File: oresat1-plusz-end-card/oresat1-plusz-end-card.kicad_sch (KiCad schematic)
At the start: 35 parts, among them J1 J-SAMTEC-TFM-120-01-L-D-RA, J2 M55-7101242R, J3 M55-7101242R, J4 M55-7101242R, J5 M55-7101242R, J6 U.FL-R-SMT-1

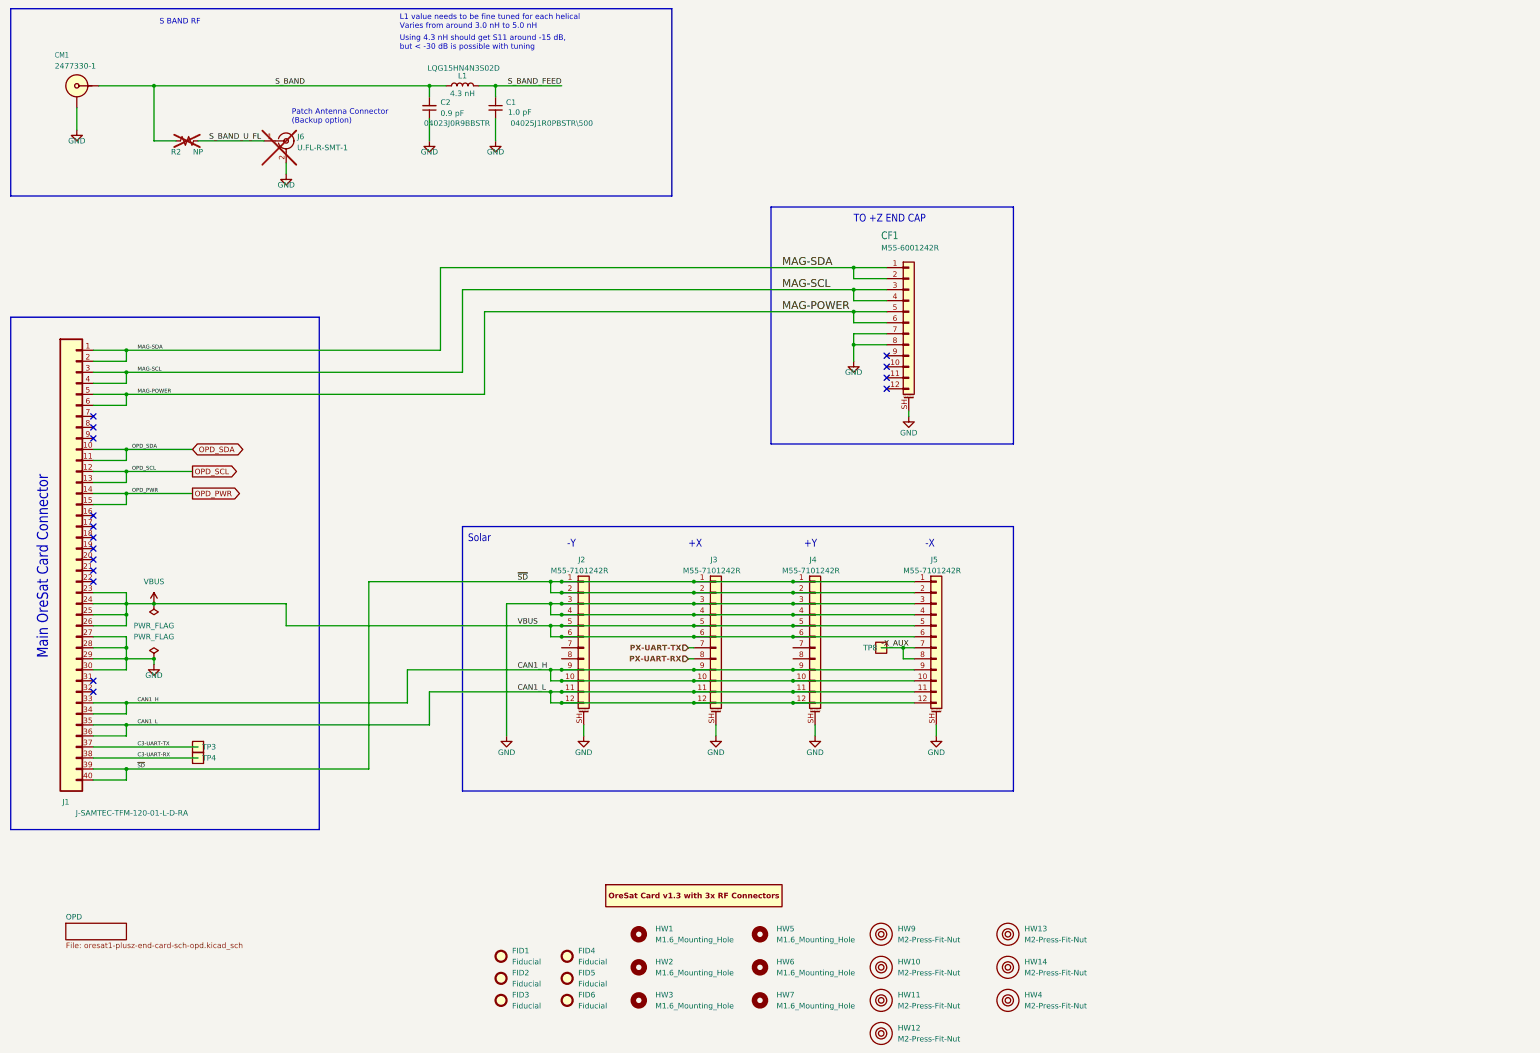
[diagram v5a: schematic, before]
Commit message: Fixed schematic label issues and routed solar uarts
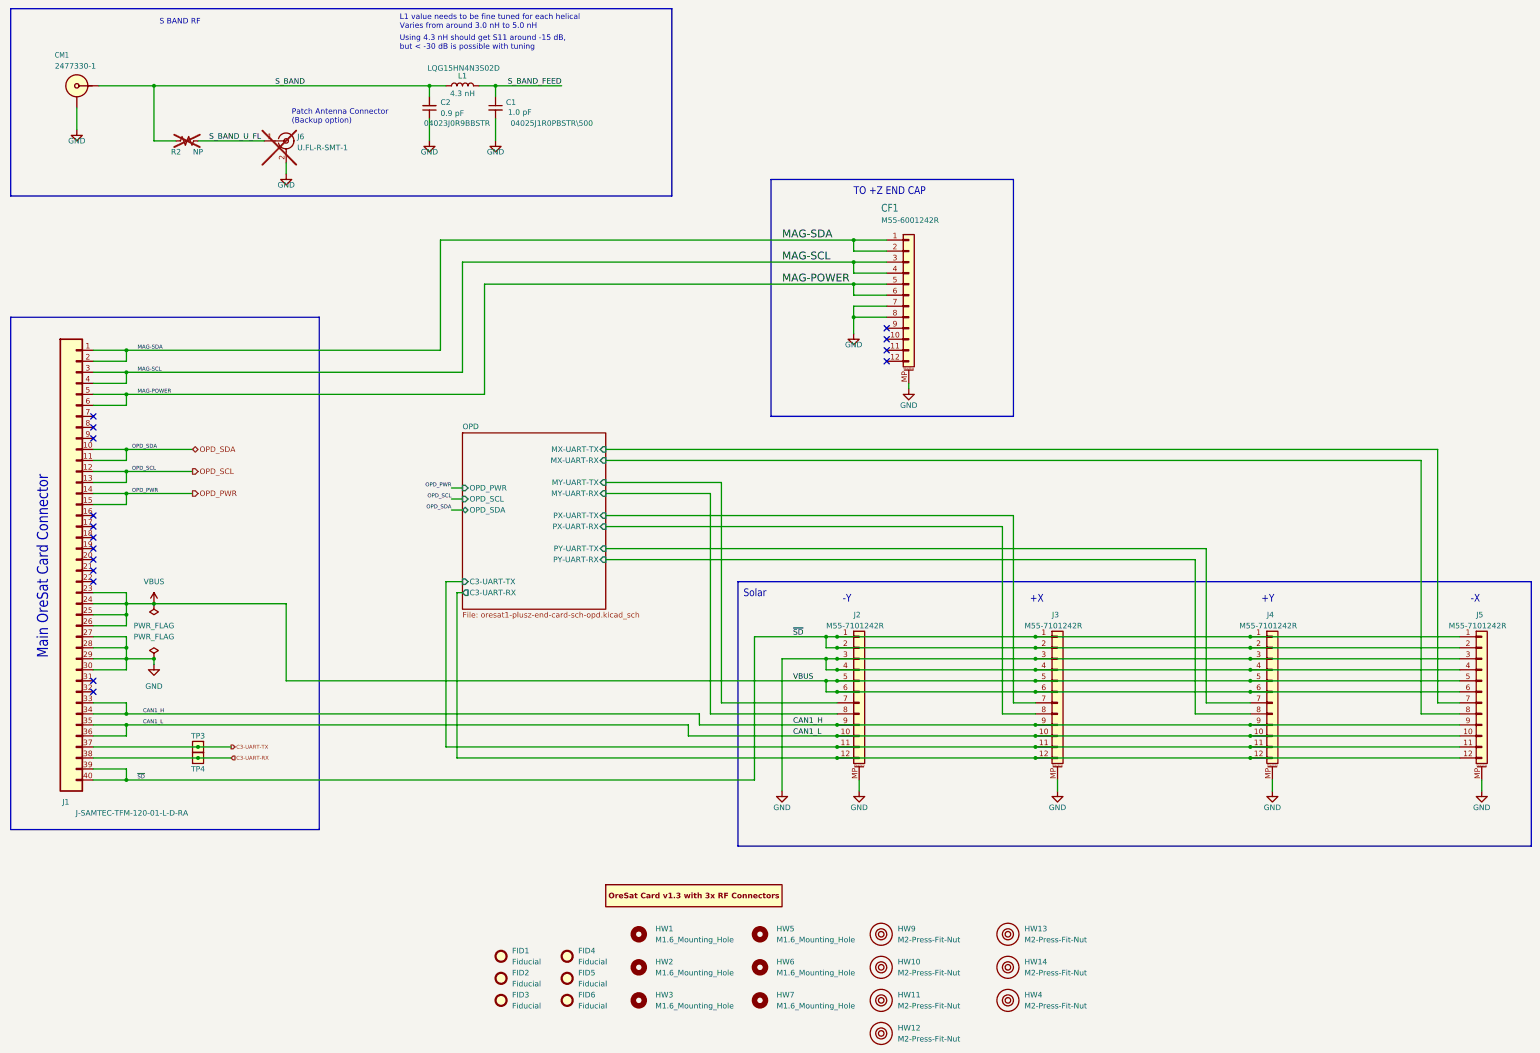
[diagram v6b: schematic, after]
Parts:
- removed TP8: TestPoint-MinTH, oresat-misc:TestPoint-0.75mm-th, symbol oresat-misc:Test-Point-0.75mm-th
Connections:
- net CAN1_H: no longer J2.10 (Pin_10), J3.10 (Pin_10), J4.10 (Pin_10), J5.10 (Pin_10)
- net CAN1_L: now also J2.10 (Pin_10), J3.10 (Pin_10), J4.10 (Pin_10), J5.10 (Pin_10); no longer J2.11 (Pin_11), J2.12 (Pin_12), J3.11 (Pin_11), J3.12 (Pin_12), J4.11 (Pin_11), J4.12 (Pin_12), J5.11 (Pin_11), J5.12 (Pin_12)
- net GND: now also CF1.MP (MountPin), J2.MP (MountPin), J3.MP (MountPin), J4.MP (MountPin), J5.MP (MountPin); no longer CF1.SH (MountPin), J2.SH (MountPin), J3.SH (MountPin), J4.SH (MountPin), J5.SH (MountPin)
- net OPD/MY-UART-TX: now reaches J2.7 (Pin_7)
- net OPD/MY-UART-RX: now reaches J2.8 (Pin_8)
- net OPD/PY-UART-TX: now reaches J4.7 (Pin_7)
- net OPD/PY-UART-RX: now reaches J4.8 (Pin_8)
- net -X_AUX renamed OPD/MX-UART-RX
- net OPD/MX-UART-RX: no longer J5.7 (Pin_7)
- net PX-UART-RX renamed OPD/PX-UART-RX
- net PX-UART-TX renamed OPD/PX-UART-TX
- new net OPD/C3-UART-RX: J2.12 (Pin_12), J3.12 (Pin_12), J4.12 (Pin_12), J5.12 (Pin_12)
- new net OPD/C3-UART-TX: J2.11 (Pin_11), J3.11 (Pin_11), J4.11 (Pin_11), J5.11 (Pin_11)
- new net OPD/MX-UART-TX: J5.7 (Pin_7)
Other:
- sheet OPD ports: added C3-UART-RX, C3-UART-TX, MX-UART-RX, MX-UART-TX, MY-UART-RX, MY-UART-TX, OPD_PWR, OPD_SCL, OPD_SDA, PX-UART-RX, PX-UART-TX, PY-UART-RX, PY-UART-TX; removed none
- moved on the sheet: CF1, J2, J3, J4, J5

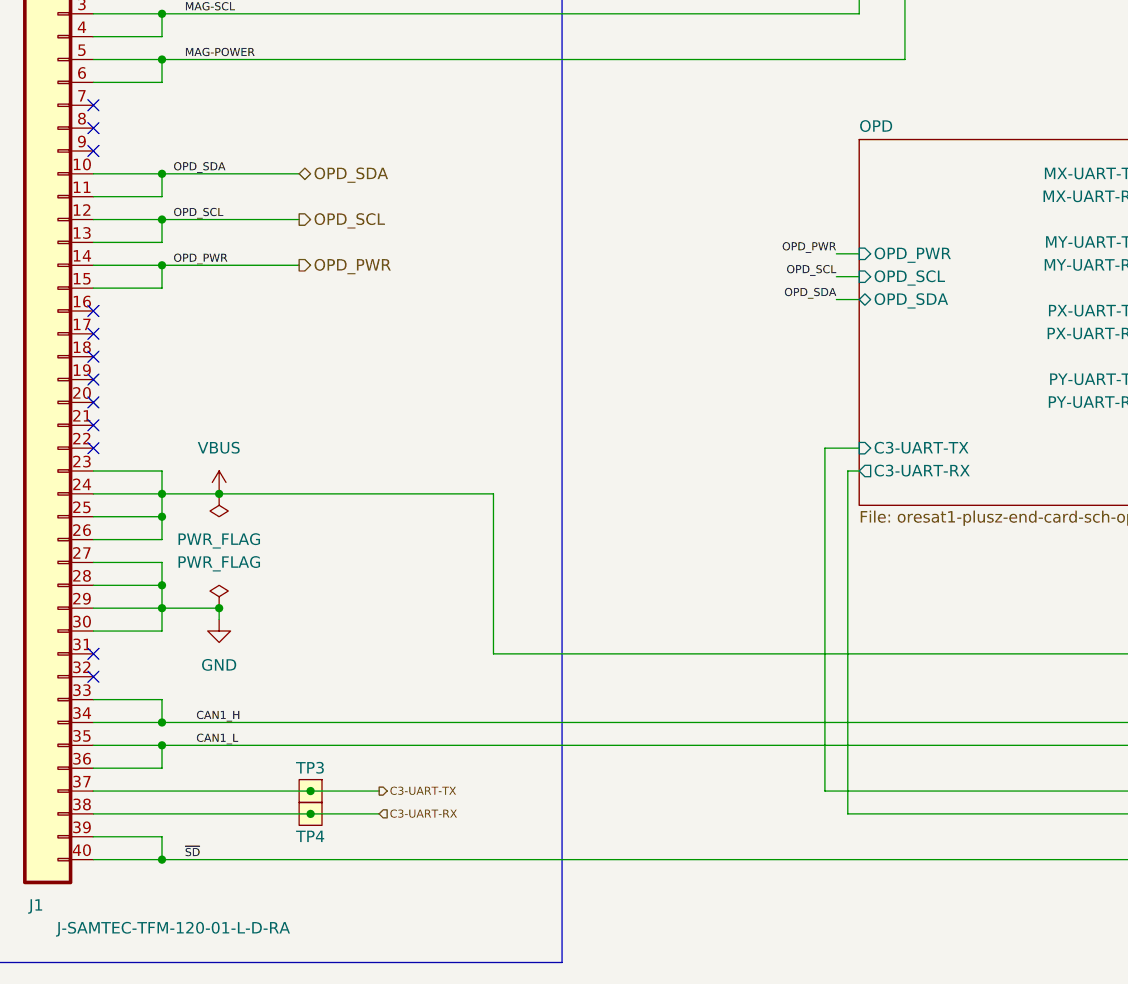
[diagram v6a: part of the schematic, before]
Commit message: fixed shcematic issues and routing, updated footprints
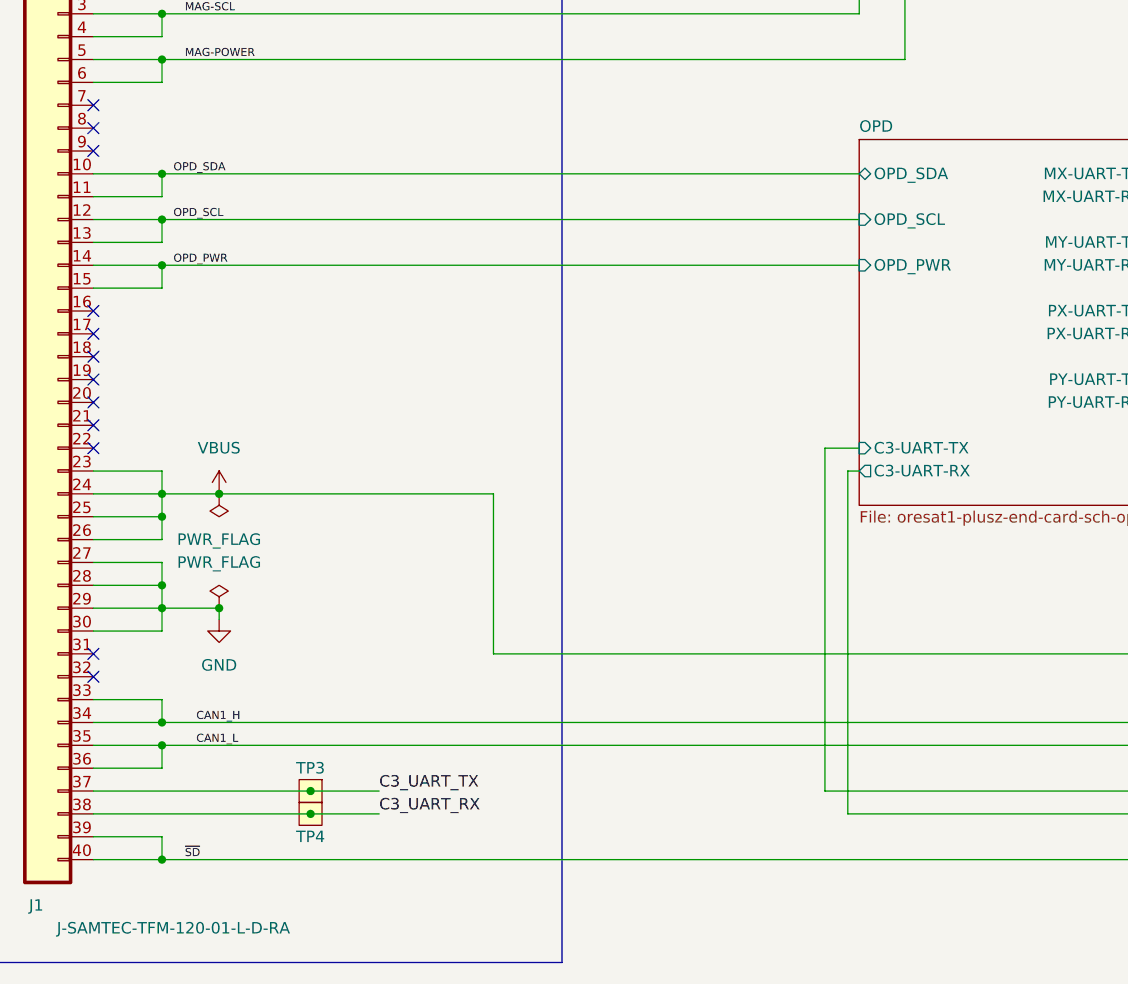
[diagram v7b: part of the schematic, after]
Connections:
- net C3-UART-RX renamed C3_UART_RX
- net C3-UART-TX renamed C3_UART_TX
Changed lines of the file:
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@@
 	(wire
 		(pts
-			(xy 74.93 119.38) (xy 90.17 119.38)
+			(xy 74.93 119.38) (xy 152.4 119.38)
 		)
 		(stroke
@@
 	(wire
 		(pts
-			(xy 74.93 124.46) (xy 90.17 124.46)
+			(xy 74.93 124.46) (xy 152.4 124.46)
 		)
 		(stroke
@@
 	(wire
 		(pts
-			(xy 149.86 130.81) (xy 152.4 130.81)
-		)
-		(stroke
-			(width 0)
-			(type default)
-		)
-	)
-	(wire
-		(pts
 			(xy 67.31 185.42) (xy 74.93 185.42)
 		)
@@
 	(wire
 		(pts
-			(xy 149.86 133.35) (xy 152.4 133.35)
-		)
-		(stroke
-			(width 0)
-			(type default)
-		)
-	)
-	(wire
-		(pts
 			(xy 74.93 104.14) (xy 74.93 101.6)
 		)
@@
 	(wire
 		(pts
-			(xy 74.93 129.54) (xy 90.17 129.54)
+			(xy 74.93 129.54) (xy 152.4 129.54)
 		)
 		(stroke
@@
 	(wire
 		(pts
-			(xy 149.86 128.27) (xy 152.4 128.27)
-		)
-		(stroke
-			(width 0)
-			(type default)
-		)
-	)
-	(wire
-		(pts
 			(xy 250.19 86.36) (xy 242.57 86.36)
 		)
@@
 		)
 	)
-	(label "OPD_SDA"
-		(at 149.86 133.35 180)
-		(effects
-			(font
-				(size 0.889 0.889)
-			)
-			(justify right bottom)
-		)
-	)
 	(label "CAN1_L"
 		(at 78.74 182.88 0)
@@
 		)
 	)
-	(label "OPD_SCL"
-		(at 149.86 130.81 180)
-		(effects
-			(font
-				(size 0.889 0.889)
-			)
-			(justify right bottom)
-		)
-	)
 	(label "~{SD}"
 		(at 228.6 162.56 0)
@@
 		)
 	)
-	(label "MAG-SDA"
-		(at 77.47 96.52 0)
+	(label "C3_UART_RX"
+		(at 99.06 190.5 0)
 		(effects
 			(font
-				(size 0.889 0.889)
+				(size 1.27 1.27)
 			)
 			(justify left bottom)
 		)
 	)
-	(label "OPD_PWR"
-		(at 149.86 128.27 180)
+	(label "MAG-SDA"
+		(at 77.47 96.52 0)
 		(effects
 			(font
 				(size 0.889 0.889)
 			)
-			(justify right bottom)
+			(justify left bottom)
 		)
 	)
@@
 		)
 	)
-	(label "CAN1_H"
-		(at 228.6 182.88 0)
-		(effects
-			(font
-				(size 1.2446 1.2446)
-			)
-			(justify left bottom)
-		)
-	)
-	(hierarchical_label "OPD_SDA"
-		(shape bidirectional)
-		(at 90.17 119.38 0)
-		(effects
-			(font
-				(size 1.27 1.27)
-			)
-			(justify left)
-		)
-	)
-	(hierarchical_label "C3-UART-TX"
-		(shape output)
+	(label "C3_UART_TX"
 		(at 99.06 187.96 0)
 		(effects
 			(font
-				(size 0.889 0.889)
-			)
-			(justify left)
-		)
-	)
-	(hierarchical_label "C3-UART-RX"
-		(shape input)
-		(at 99.06 190.5 0)
-		(effects
-			(font
-				(size 0.889 0.889)
-			)
-			(justify left)
-		)
-	)
-	(hierarchical_label "OPD_PWR"
-		(shape output)
-		(at 90.17 129.54 0)
-		(effects
-			(font
 				(size 1.27 1.27)
 			)
-			(justify left)
+			(justify left bottom)
 		)
 	)
-	(hierarchical_label "OPD_SCL"
-		(shape output)
-		(at 90.17 124.46 0)
+	(label "CAN1_H"
+		(at 228.6 182.88 0)
 		(effects
 			(font
-				(size 1.27 1.27)
+				(size 1.2446 1.2446)
 			)
-			(justify left)
+			(justify left bottom)
 		)
 	)
@@
 		)
 		(pin "OPD_PWR" input
-			(at 152.4 128.27 180)
+			(at 152.4 129.54 180)
 			(effects
 				(font
@@
 		)
 		(pin "OPD_SCL" input
-			(at 152.4 130.81 180)
+			(at 152.4 124.46 180)
 			(effects
 				(font
@@
 		)
 		(pin "OPD_SDA" bidirectional
-			(at 152.4 133.35 180)
+			(at 152.4 119.38 180)
 			(effects
 				(font
